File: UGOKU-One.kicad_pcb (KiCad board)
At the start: 2 copper layers, 70 x 70 mm, 82 parts, among them J1 ENC/IO, J10 Conn_01x02, J11 USB_C_Receptacle_USB2.0_16P, J12 Conn_01x02, J2 SERVO, J3 Conn_02x03_Odd_Even, J4 14110213001000, J5 Conn_01x05, J6 Conn_01x02, J7 ENC/IO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

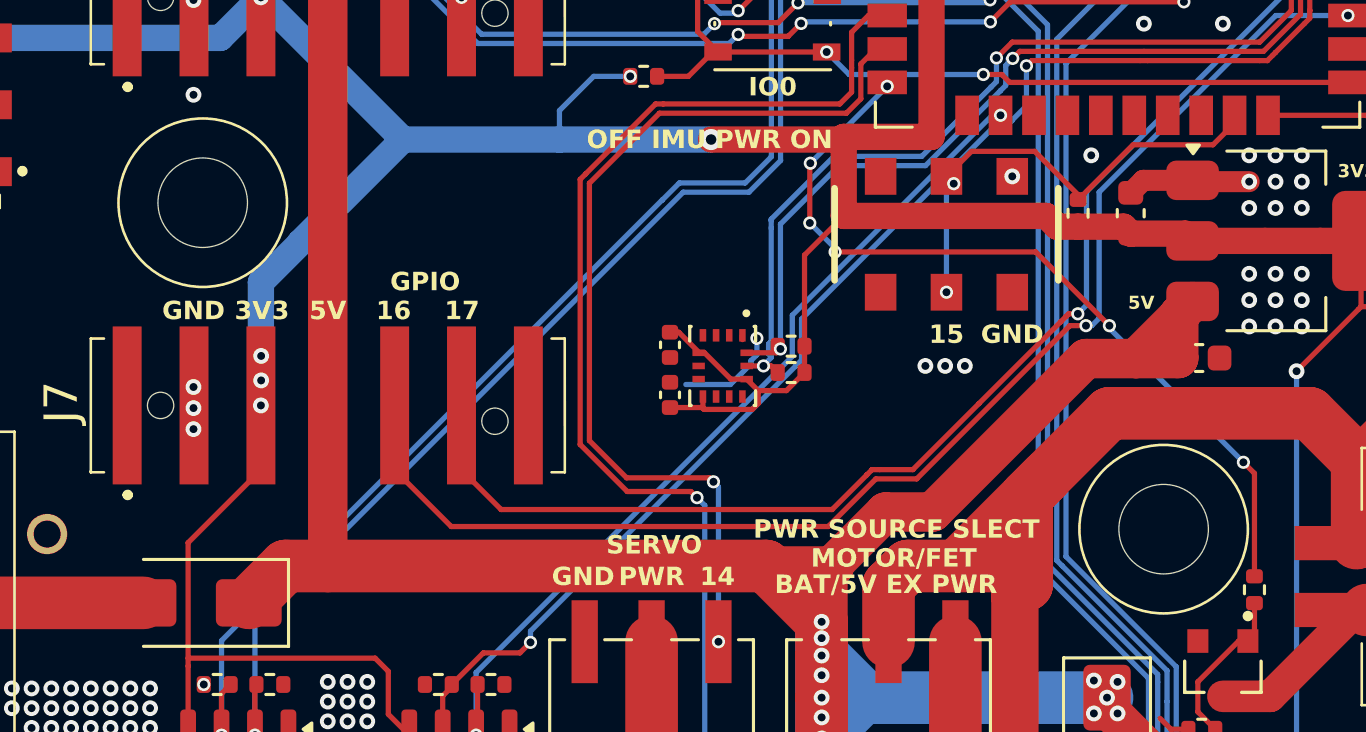
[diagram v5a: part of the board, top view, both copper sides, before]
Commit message: 電池ボックスボルトをM2.6に変更 JLCPCB tool 部品表の部品座標、向きを修正
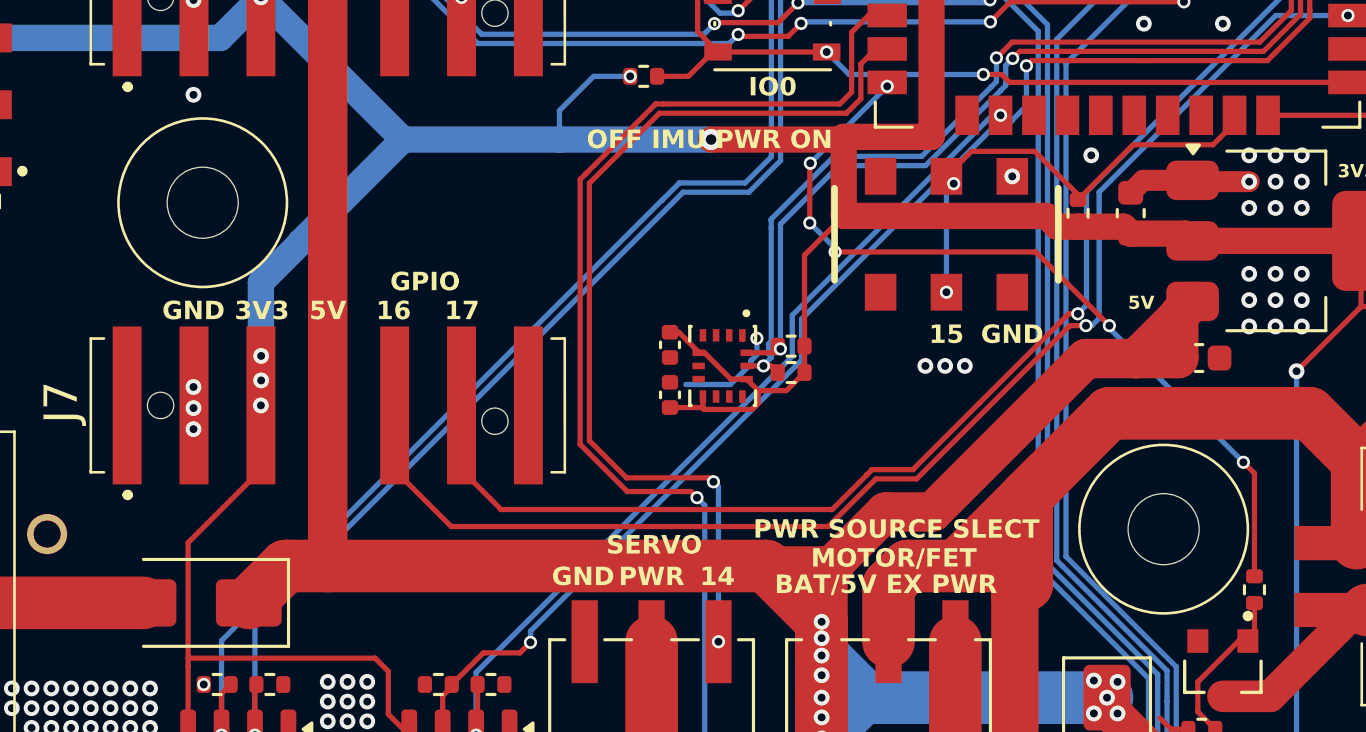
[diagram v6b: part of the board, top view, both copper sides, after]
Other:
- board text added: "UGOKU One Ver 1.1.1 UGOKU Lab 2025-8"
- board text removed: "UGOKU One Ver1.1.1 UGOKU Lab 2025-6"
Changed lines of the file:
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@@
 			(psa4output no)
 			(plot_black_and_white no)
-			(plotinvisibletext no)
 			(sketchpadsonfab no)
 			(plotpadnumbers no)
@@
 		(sheetname "/")
 		(sheetfile "UGOKU-One.kicad_sch")
-		(attr through_hole exclude_from_pos_files)
+		(attr through_hole)
 		(fp_circle
 			(center 18.25 6.2)
@@
 		(pad "" np_thru_hole circle
 			(at -18.25 -6.2 180)
-			(size 3.4 3.4)
-			(drill 3.4)
+			(size 2.7 2.7)
+			(drill 2.7)
 			(layers "*.Cu" "*.Mask")
 			(clearance 1.5)
@@
 		(pad "" np_thru_hole circle
 			(at 18.25 6.2 180)
-			(size 3.4 3.4)
-			(drill 3.4)
+			(size 2.7 2.7)
+			(drill 2.7)
 			(layers "*.Cu" "*.Mask")
 			(clearance 1.5)
@@
 		)
 	)
-	(gr_text "UGOKU One Ver1.1.1 UGOKU Lab 2025-6\n"
+	(gr_text "UGOKU One Ver 1.1.1 UGOKU Lab 2025-8\n"
 		(at 33.75 1.25 90)
 		(layer "B.SilkS")

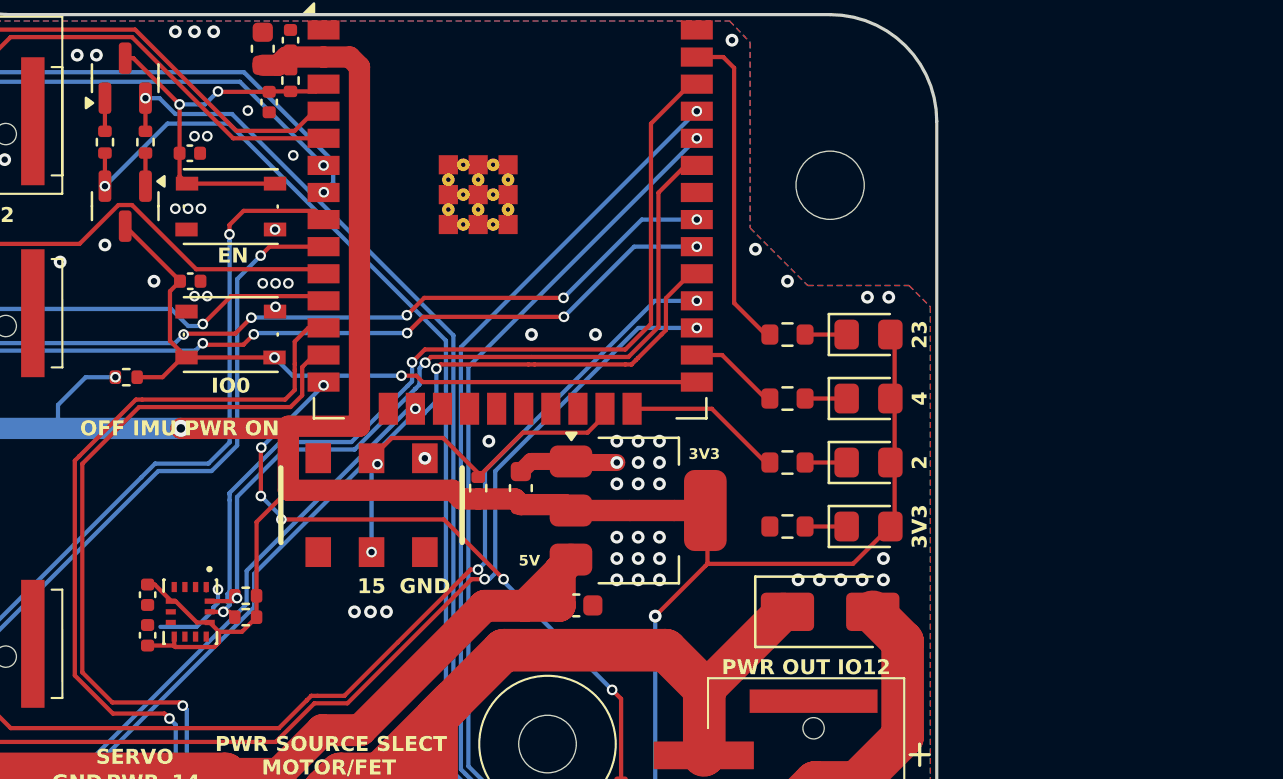
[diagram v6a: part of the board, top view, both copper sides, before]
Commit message: JLCPCB economy に対応するためIMUをICM-42605に変更
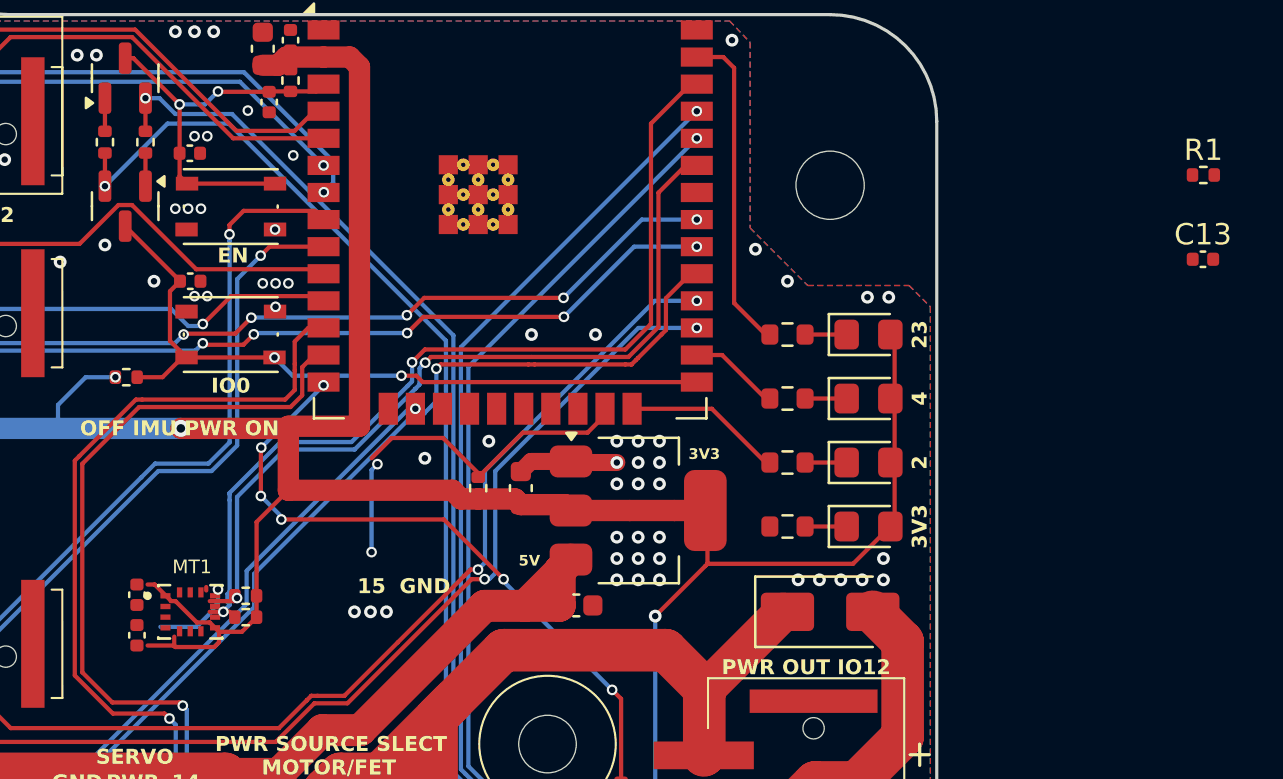
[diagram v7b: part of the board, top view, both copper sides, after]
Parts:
- removed SW3: SW_Slide_DPDT, 0_UGOKU-One_Lib:SSSS213202
- removed U7: BMI270, 0_UGOKU-One_Lib:XDCR_BMI270
- added C13: 10nF, Capacitor_SMD:C_0402_1005Metric, F.Cu at (47.5, -16.5)
- added MT1: ICM-42605, 0_UGOKU-One_Lib:XDCR_ICM-42605, F.Cu at (0.00, 0.00)
- added R1: 10k, Resistor_SMD:R_0402_1005Metric, F.Cu at (47.5, -20.5)
- C15: value 0.1uF -> 2.2uF
- moved C14 0.50 mm to (-2.50, -0.80)
- moved C15 0.50 mm to (-2.50, 1.10)
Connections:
- R22 pad 2: Slide_SW -> SW_DIP_1
- U5 pad 6: IO34 -> INT1
- U5 pad 7: IO35 -> INT2

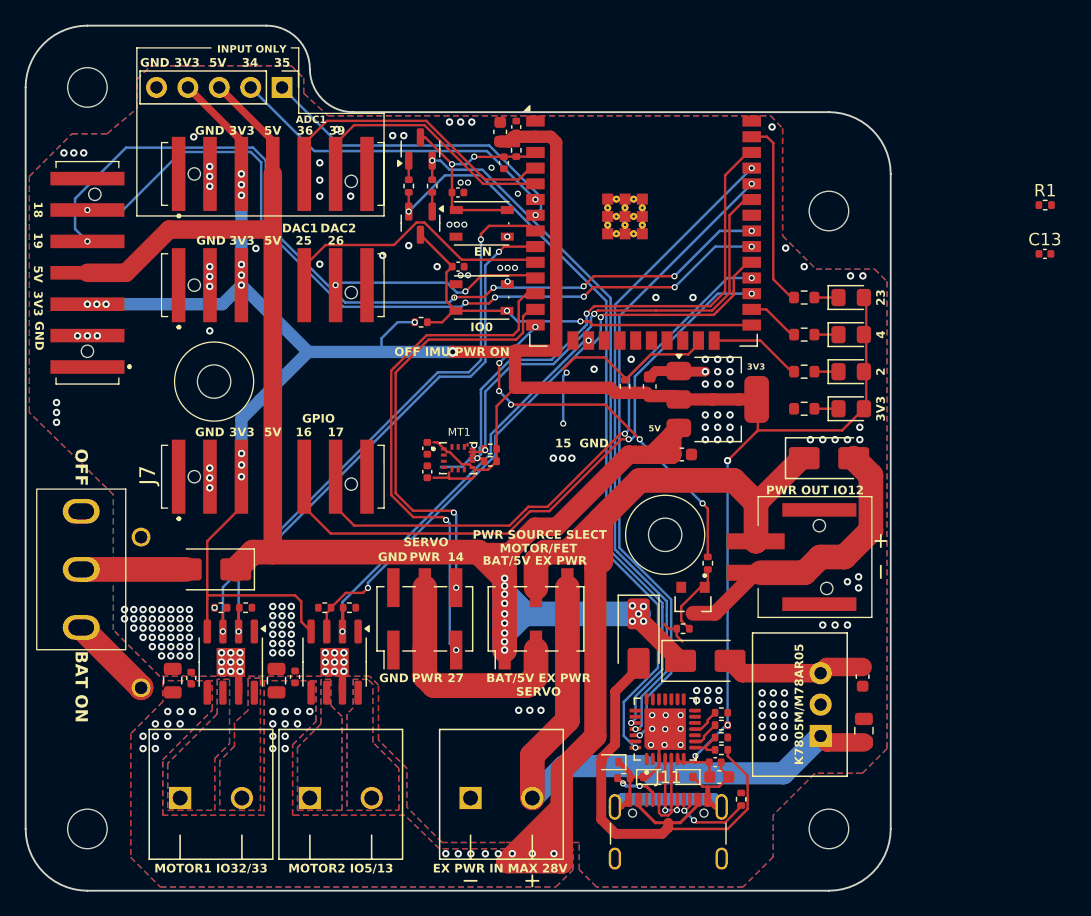
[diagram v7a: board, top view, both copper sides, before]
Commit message: ピン配置とコネクタ配置を変更
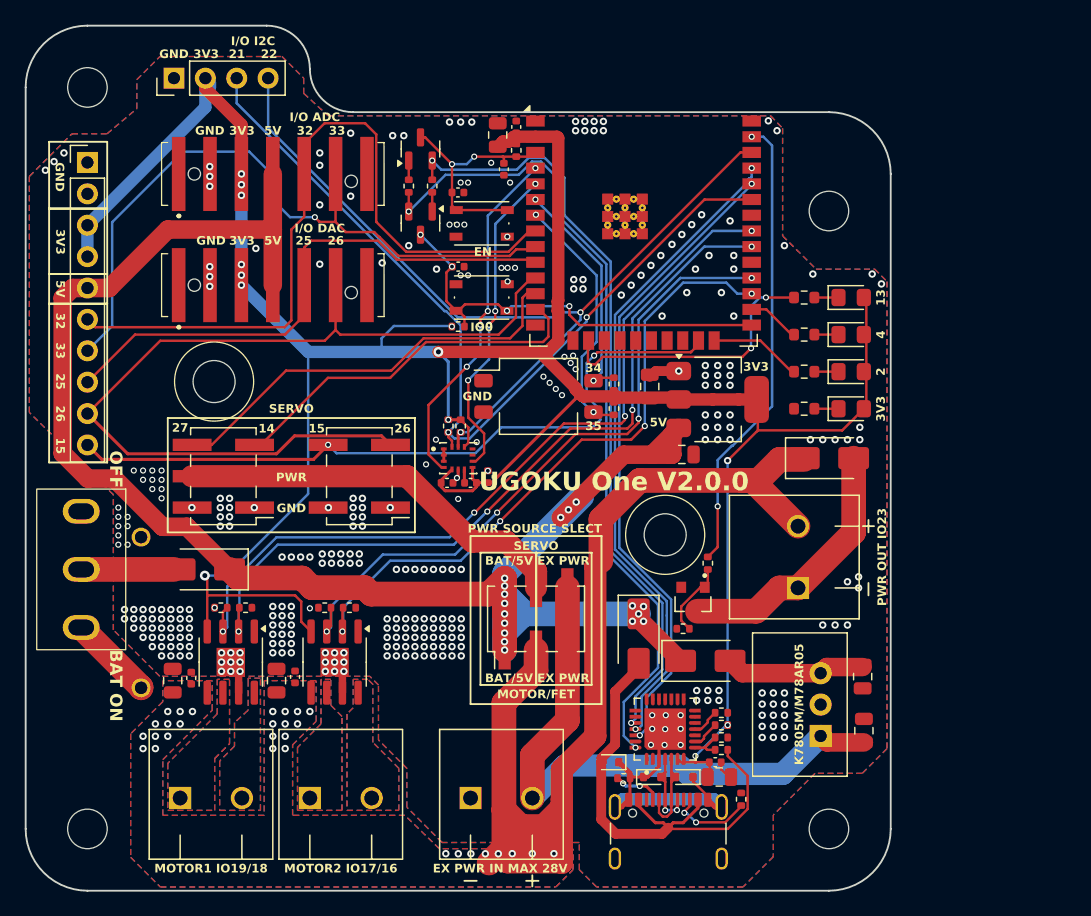
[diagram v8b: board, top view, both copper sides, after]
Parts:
- removed J7: ENC/IO, 0_UGOKU-One_Lib:14110513001000
- added J13: Conn_01x02, 0_UGOKU-One_Lib:PTS_1.5_2, F.Cu at (27.5, 8.00)
- added SW1: SW_DIP_x02, Button_Switch_SMD:SW_DIP_SPSTx02_Slide_Omron_A6S-210x_W8.9mm_P2.54mm, F.Cu at (6.50, -5.00)
- C1, C10, C11, C2, C5: footprint Capacitor_SMD:C_0603_1608Metric -> Capacitor_SMD:C_0805_2012Metric
- J1: value ENC/IO -> Conn_01x04; footprint 0_UGOKU-One_Lib:14110513001000 -> Connector_PinHeader_2.54mm:PinHeader_1x04_P2.54mm_Vertical
- J4: value 14110213001000 -> Conn_01x10; footprint 0_UGOKU-One_Lib:14010213102000 -> Connector_PinHeader_2.54mm:PinHeader_1x10_P2.54mm_Vertical
- J5: value Conn_01x05 -> SERVO; footprint Connector_PinHeader_2.54mm:PinHeader_1x05_P2.54mm_Vertical -> Connector_PinHeader_2.54mm:PinHeader_2x03_P2.54mm_Vertical_SMD
- R23: value 10k -> 100k
- moved J4 65.9 mm to (-30.0, -23.9), turned to 0 degrees
- moved C13 51.8 mm to (-0.90, 2.00)
- moved R1 38.6 mm to (12.6, -4.01), turned to -90 degrees
- moved J5 32.1 mm to (-8.00, 1.46), turned to 180 degrees
- moved J2 20.0 mm to (-19.0, 1.46), turned to 180 degrees
- moved J1 17.2 mm to (-23.0, -30.8)
- moved C15 4.92 mm to (2.40, 1.50)
- moved C14 4.48 mm to (1.00, 2.00), turned to 180 degrees
- moved R28 3.87 mm to (-0.80, -2.60), turned to -90 degrees
- moved R27 3.73 mm to (0.20, -2.60), turned to -90 degrees
- moved R32 3.02 mm to (0.00, -10.7)
- moved R22 0.92 mm to (12.6, -6.00)
- moved C12 0.52 mm to (3.70, -23.4)
- moved D6 0.50 mm to (-20.5, 9.00)
- moved C5 0.32 mm to (3.20, -26.1)
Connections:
- J1 pad 3: 5V -> SDA
- J1 pad 4: IO19 -> SCL
- J3 pad 3: SERVO_PWR -> MOT_PWR
- J3 pad 4: MOT_PWR -> SERVO_PWR
- J4 pad 1: MOT_PWR -> GND
- J4 pad 2: Net-(D8-A) -> GND
- J4 pad 3: unconnected-(J4-Pad3) -> 3V3
- J4 pad 4: unconnected-(J4-Pad4) -> 3V3
- J5 pad 1: IO35 -> GND
- J5 pad 2: IO34 -> GND
- J5 pad 3: 5V -> SERVO_PWR
- J5 pad 4: 3V3 -> SERVO_PWR
- J5 pad 5: GND -> DAC2
- J9 pad 4: SENS_VP -> ADC1
- J9 pad 5: SENS_VN -> ADC2
- R1 pad 2: (no net) -> SW_DIP_2
- U5 pad 12: SERVO2 -> SERVO1
- U5 pad 13: SERVO1 -> SERVO2
- U5 pad 14: FET_SW -> unconnected-(U5-IO12-Pad14)
- U5 pad 16: MD2_IN2 -> LED3
- U5 pad 23: Slide_SW -> IO15
- U5 pad 27: IO16 -> MD2_IN2
- U5 pad 28: IO17 -> MD2_IN1
- U5 pad 29: MD2_IN1 -> unconnected-(U5-IO5-Pad29)
- U5 pad 30: IO18 -> MD1_IN2
- U5 pad 31: IO19 -> MD1_IN1
- U5 pad 37: LED3 -> FET_SW
- U5 pad 4: SENS_VP -> INT1
- U5 pad 5: SENS_VN -> INT2
- U5 pad 6: INT1 -> SW_DIP_1
- U5 pad 7: INT2 -> SW_DIP_2
- U5 pad 8: MD1_IN1 -> ADC1
- U5 pad 9: MD1_IN2 -> ADC2
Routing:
- net IO19: track 70.9 -> 0.00 mm, vias 6 -> 0
- net IO18: track 65.9 -> 0.00 mm, vias 6 -> 0
- net ADC1: track 0.00 -> 60.3 mm
- net IO15: track 0.00 -> 58.9 mm, vias 0 -> 2
- net ADC2: track 0.00 -> 56.7 mm, vias 0 -> 1
- net DAC2: track 17.3 -> 72.6 mm, vias 2 -> 0
- net IO16: track 51.0 -> 0.00 mm, vias 2 -> 0
- net IO17: track 47.6 -> 0.00 mm, vias 2 -> 0
- net SDA: track 38.3 -> 70.9 mm
- net INT1: track 0.00 -> 28.4 mm, vias 0 -> 4
- net SCL: track 43.0 -> 70.4 mm
- net IO34: track 26.8 -> 0.00 mm, vias 1 -> 0
- net IO35: track 26.3 -> 0.00 mm, vias 1 -> 0
- net INT2: track 0.00 -> 25.8 mm, vias 0 -> 4
- net SENS_VP: track 24.3 -> 0.00 mm
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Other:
- board text added: "13"
- board text added: "21"
- board text added: "22"
- board text added: "32"
- board text added: "33"
- board text added: "I/O ADC"
- board text added: "I/O DAC"
- board text added: "I/O I2C"
- board text added: "MOTOR1 IO19/18"
- board text added: "MOTOR2 IO17/16"
- board text added: "PWR OUT IO23"
- board text added: "UGOKU One V2.0.0"
- board text added: "UGOKU One Ver 2.0.0 UGOKU Lab 2025-8"
- board text removed: "16"
- board text removed: "17"
- board text removed: "18"
- board text removed: "19"
- board text removed: "23"
- board text removed: "36"
- board text removed: "39"
- board text removed: "ADC1"
- board text removed: "DAC1"
- board text removed: "DAC2"
- board text removed: "GPIO"
- board text removed: "INPUT ONLY"
- board text removed: "MOTOR1 IO32/33"
- board text removed: "MOTOR2 IO5/13"
- board text removed: "OFF IMU PWR ON"
- board text removed: "PWR OUT IO12"
- board text removed: "UGOKU One Ver 1.1.1 UGOKU Lab 2025-8"
